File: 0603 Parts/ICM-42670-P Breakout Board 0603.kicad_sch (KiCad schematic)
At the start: 12 parts, among them J2 Conn_01x09_Pin, U1 ICM-42670-P, U3 MCP1700x-300xxTT

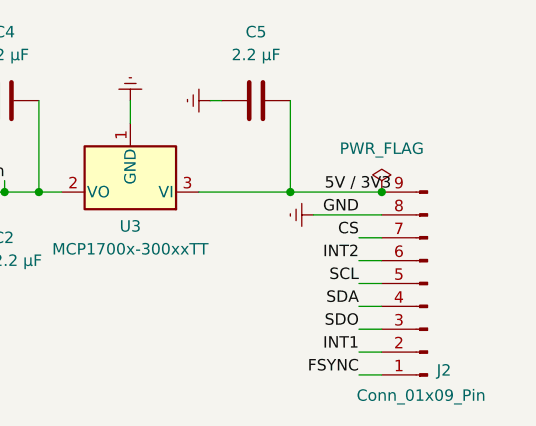
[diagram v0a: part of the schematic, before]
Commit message: DNP update on connector x9 pins
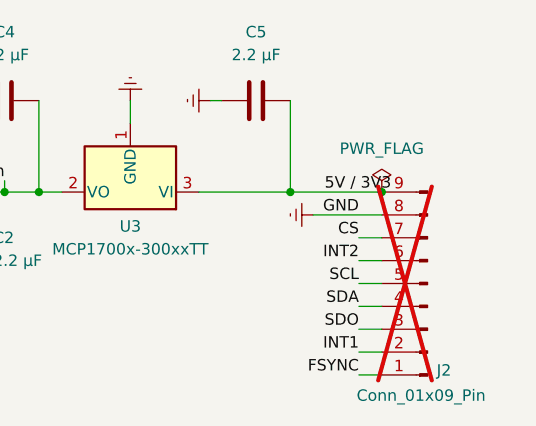
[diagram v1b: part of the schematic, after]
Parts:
- J2: now not fitted
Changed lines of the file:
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@@
 		(in_bom yes)
 		(on_board yes)
-		(dnp no)
+		(dnp yes)
 		(property "Reference" "J2"
 			(at 230.886 78.232 0)

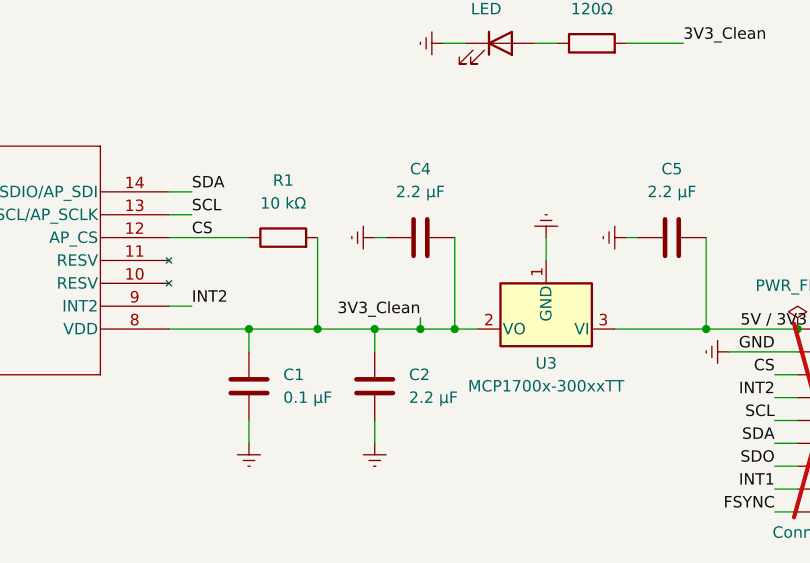
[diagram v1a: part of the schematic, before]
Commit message: Updated PCB and Schematic to include Pull Ups for SCK SDA I2c
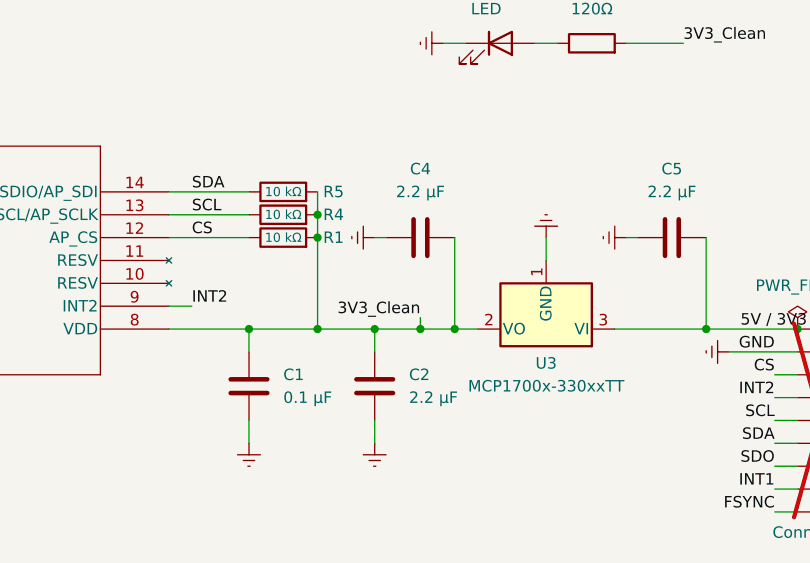
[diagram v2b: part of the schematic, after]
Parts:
- added R4, R5: 10 kΩ, Resistor_SMD:R_0603_1608Metric, symbol Device:R
- U3: value MCP1700x-300xxTT -> MCP1700x-330xxTT
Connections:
- net 3V3_Clean: now also R4.2, R5.2
- net SCL: now also R4.1
- net SDA: now also R5.1

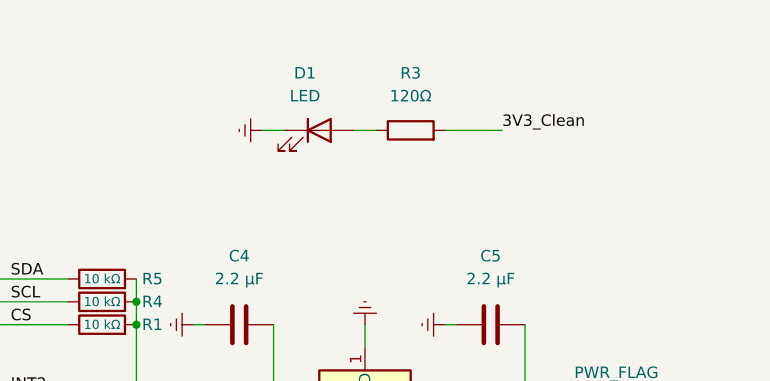
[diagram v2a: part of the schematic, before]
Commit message: Clean up redundant Traces / tracks
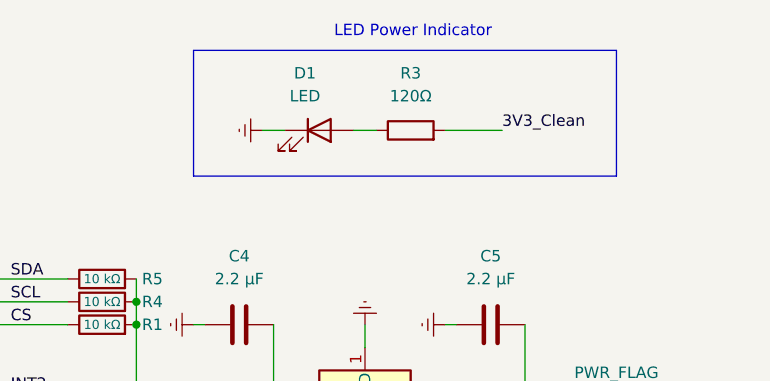
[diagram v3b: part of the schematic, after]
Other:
- note added: "LED Power Indicator"
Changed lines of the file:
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@@
 	(title_block
 		(title "ICM-42670-P Motion Sensor Breakout with Power Regulation")
-		(date "2026-MARCH-07")
+		(date "2026-March-26")
 		(rev "v1.2")
 		(company "Anthony Hua / SleepPandas")
 	)
+	(rectangle
+		(start 177.8 17.78)
+		(end 224.79 31.75)
+		(stroke
+			(width 0)
+			(type default)
+		)
+		(fill
+			(type none)
+		)
+	)
+	(text "LED Power Indicator"
+		(exclude_from_sim no)
+		(at 202.184 15.748 0)
+		(effects
+			(font
+				(size 1.27 1.27)
+			)
+		)
+	)
 	(junction
